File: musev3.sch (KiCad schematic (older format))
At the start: 82 parts, among them CON1 RCA_conn_x2, CON2 3.5mm_conn_tip_switch, CON3 3.5mm_conn_tip_switch, J1 RJ45-TRANSFO, P1 PWR_IN_PINS, P2 RF_DEBUG, P3 LED_CONN, P4 UART_CONN, P5 SMA, SW1 UART_DEBUG, SW2 RST, U1 74HC04, U2 R1171S331B, U3 GTL2010, U4 onion_omega2, U5 LM2662, U6 PCM3060, U7 RFM69HCW, X1 CFPS-73 - 24.567MHz

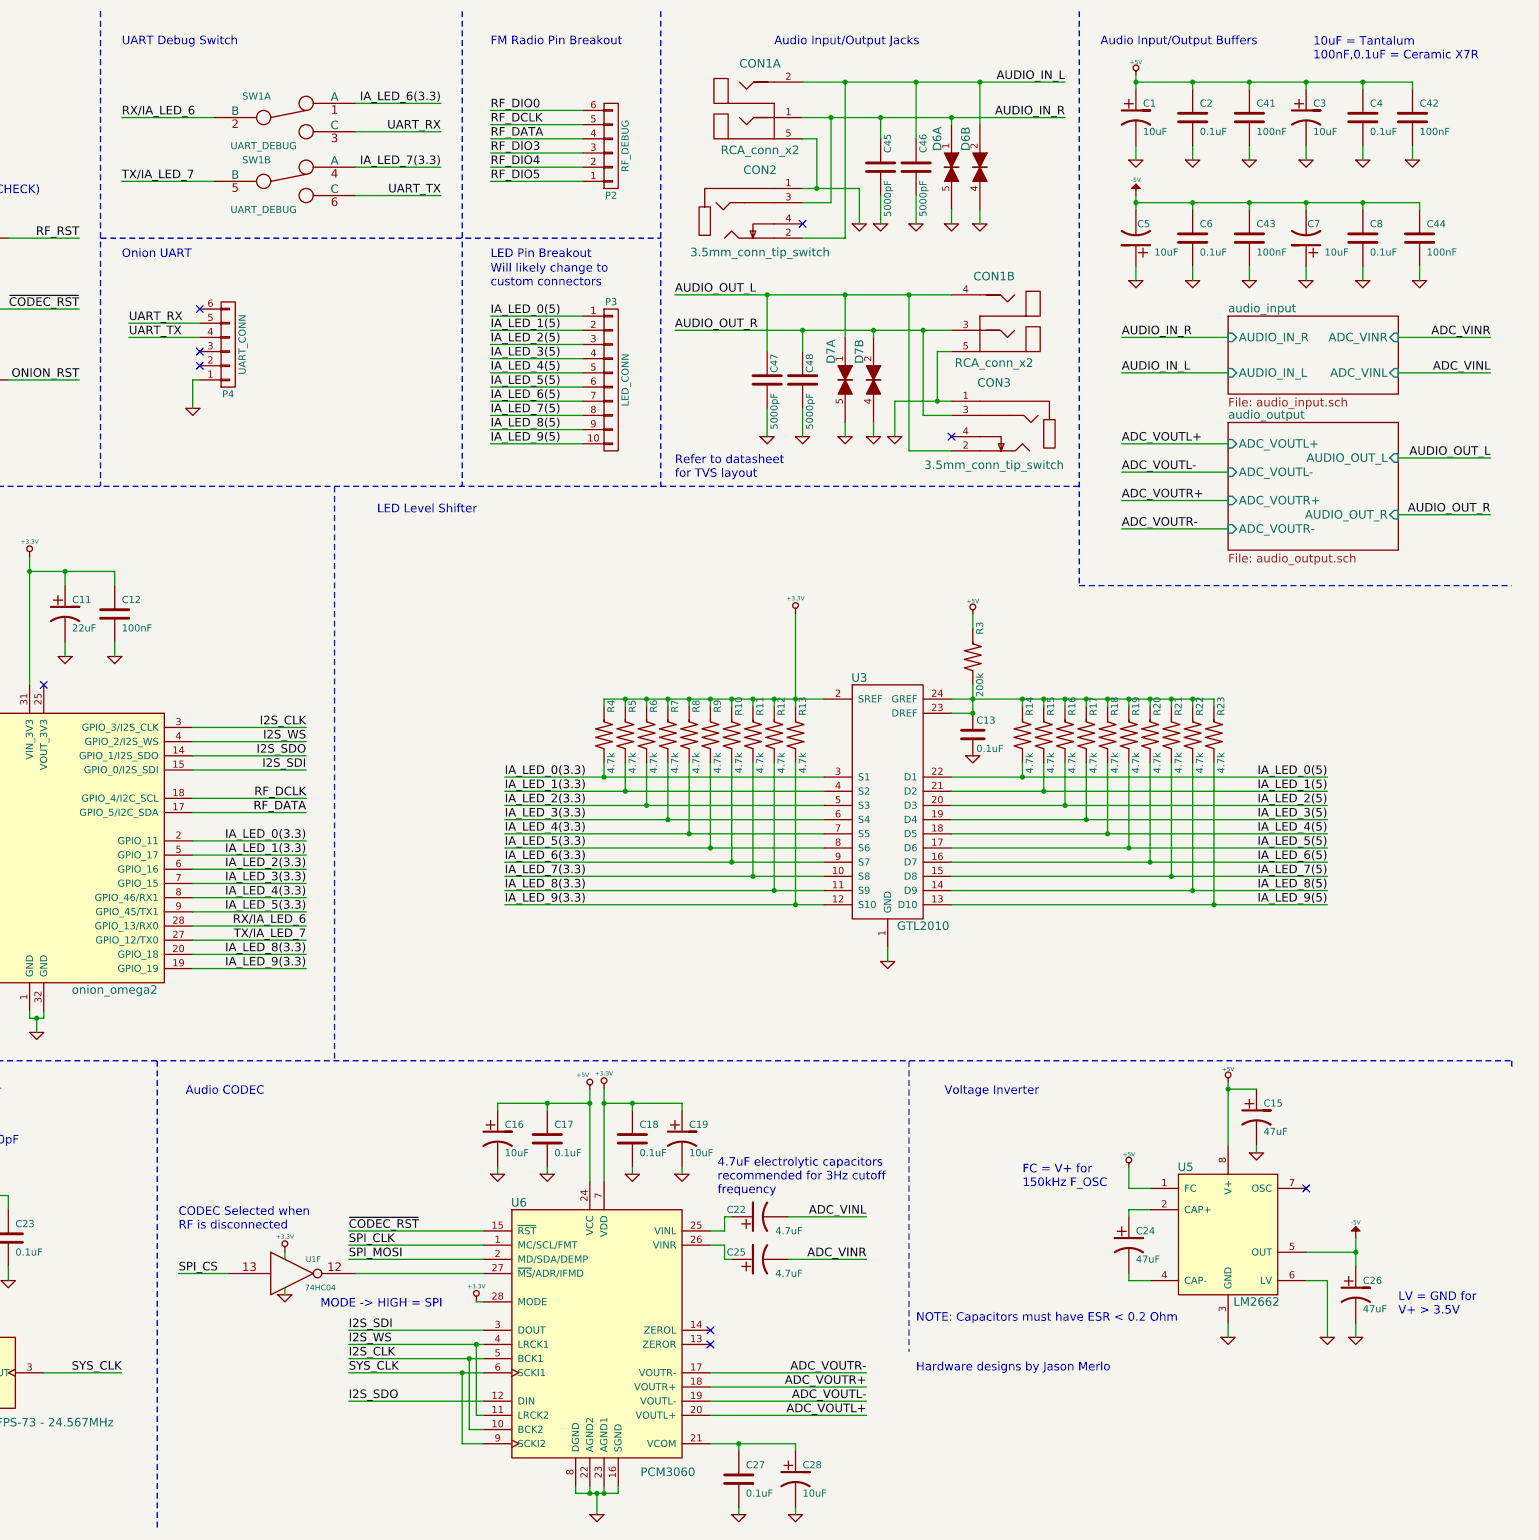
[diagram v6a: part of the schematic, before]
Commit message: Fixed decoupling cap polarity on output op-amp, added bias to analog input, changed capacitor footprints to reflect new capacitor selections
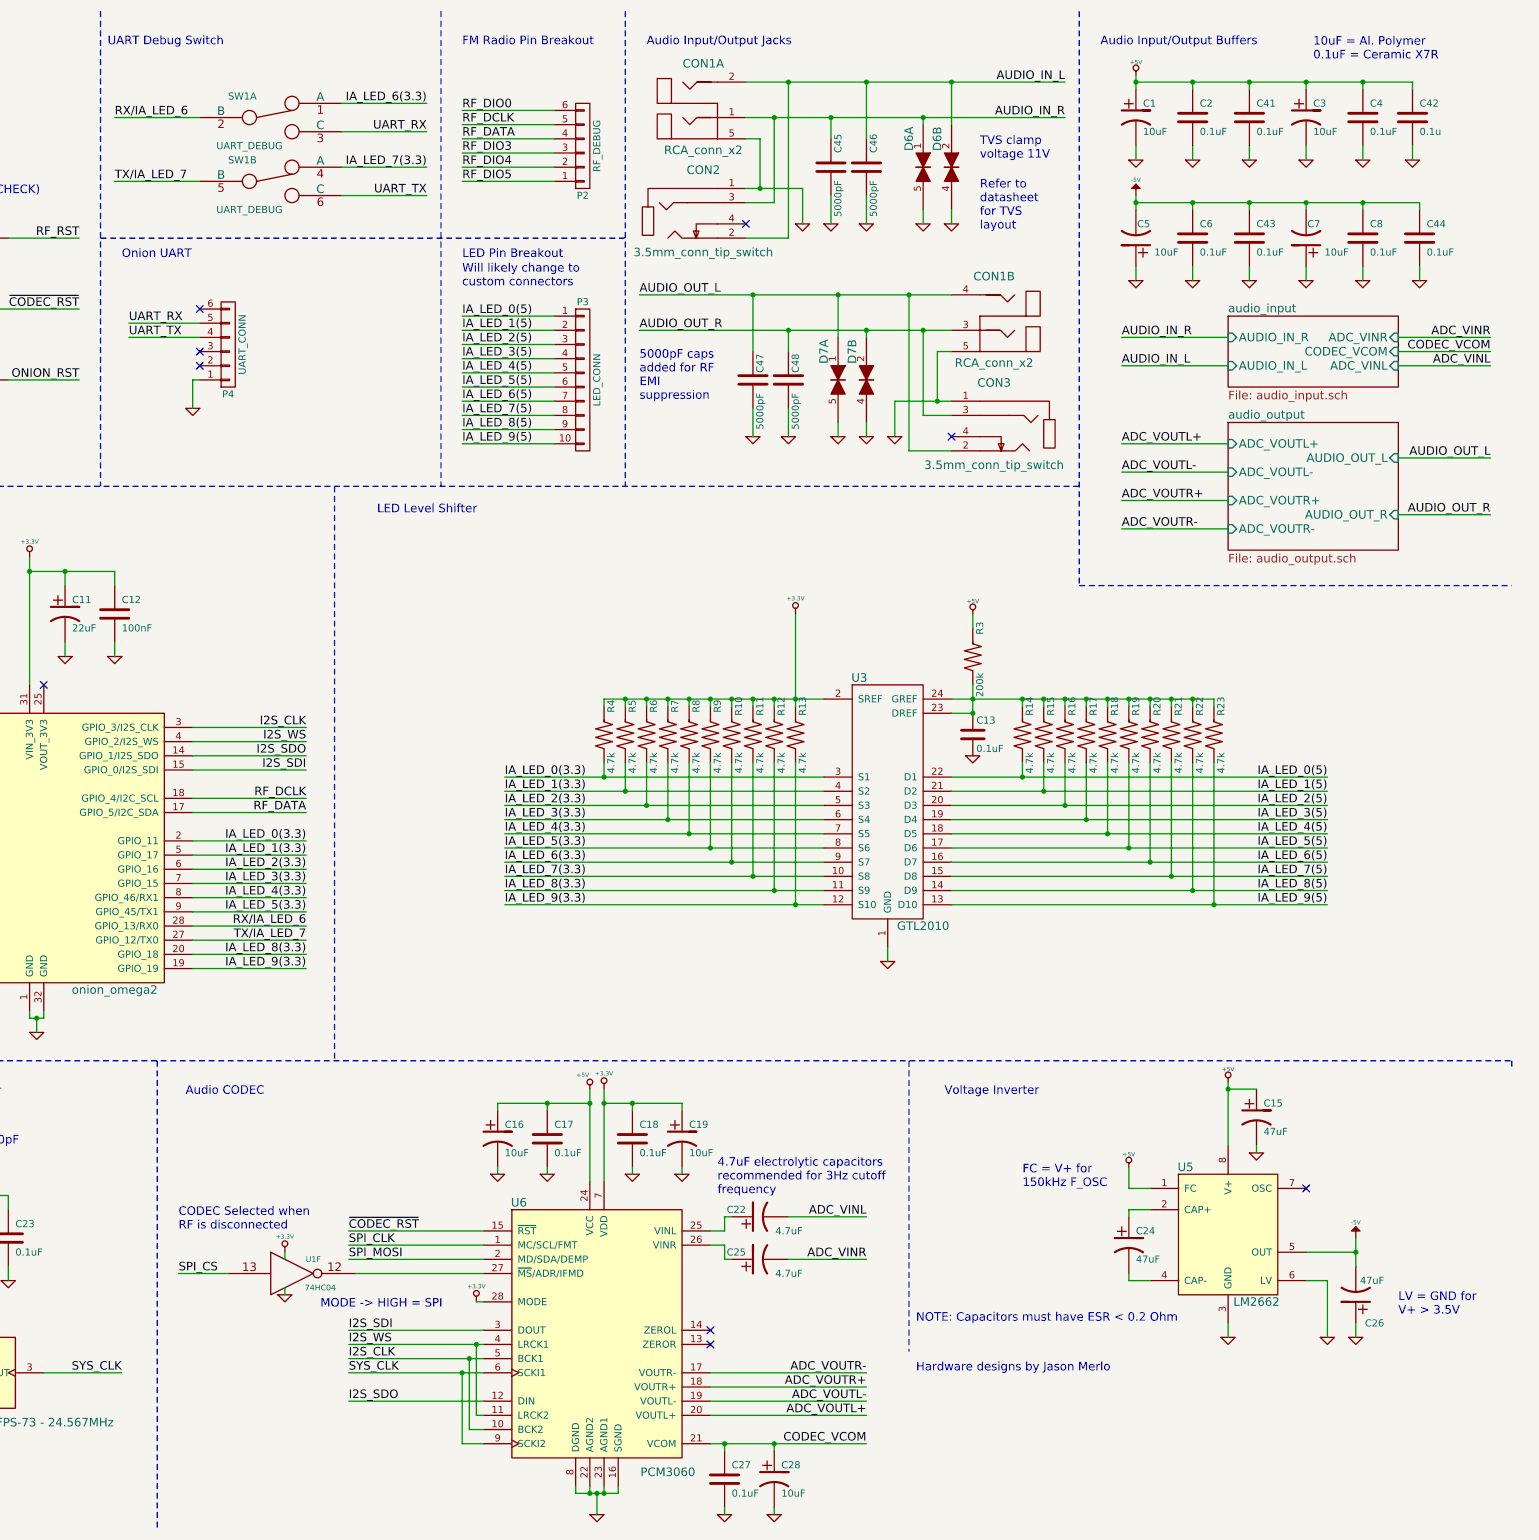
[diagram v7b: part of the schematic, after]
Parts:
- C1, C3, C5, C7: footprint Capacitors_SMD:C_0805_HandSoldering -> Capacitors_SMD:c_elec_6.3x5.7
- C11, C12, C13, C14, C17, C18, C20, C21, C23, C27: footprint (none) -> Capacitors_SMD:C_0805_HandSoldering
- C15, C19, C24, C26: footprint (none) -> Capacitors_SMD:c_elec_5x5.3
- C16, C28: footprint (none) -> Capacitors_SMD:c_elec_6.3x5.7
- C2, C4, C6, C8: footprint Capacitors_SMD:C_1206_HandSoldering -> Capacitors_SMD:C_0805_HandSoldering
- C41, C43, C44: value 100nF -> 0.1uF; footprint Capacitors_SMD:C_1206_HandSoldering -> Capacitors_SMD:C_0805_HandSoldering
- C42: value 100nF -> 0.1u; footprint Capacitors_SMD:C_1206_HandSoldering -> Capacitors_SMD:C_0805_HandSoldering
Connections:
- net -5V: now also C26.2; no longer C26.1
- net GND: now also C26.1; no longer C26.2
- net CODEC_VCOM: now reaches C27.1, C28.1, U6.21 (VCOM)
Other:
- note added: "10uF = Al. Polymer\n0.1uF = Ceramic X7R"
- note added: "5000pF caps\nadded for RF\nEMI \nsuppression"
- note added: "Refer to \ndatasheet\nfor TVS \nlayout"
- note added: "TVS clamp\nvoltage 11V"
- note removed: "10uF = Tantalum\n100nF,0.1uF = Ceramic X7R"
- note removed: "Refer to datasheet\nfor TVS layout"
- moved on the sheet: C27, C28, C45, C46, C47, C48, CON1A, CON2, D6A, D6B, D7A, D7B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

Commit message: Updated audio capacitor types to reflect BOM
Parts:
- removed C22, C25: 4.7uF, symbol CP1
- added C22, C25: 4.7uF, Capacitors_SMD:C_0805_HandSoldering, symbol C
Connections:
- net ADC_VINL: now also C22.2
- net ADC_VINR: now also C25.2
- net at U6.25 (VINL): now also C22.1
- net at U6.26 (VINR): now also C25.1
